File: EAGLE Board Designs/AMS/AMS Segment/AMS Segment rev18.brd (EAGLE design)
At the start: 275.2 x 86 mm, 345 parts, among them J1 CONNECTOR-2_MICROFIT_SMD_RIGH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, J10 CONNECTOR-2_MICROFIT_SMD_RIGH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, J100 CONNECTOR-1_5222, J101 CONNECTOR-1_5222, J102 CONNECTOR-1_5222, J103 CONNECTOR-1_5222, J104 CONNECTOR-1_5222, J105 CONNECTOR-1_5222, J106 CONNECTOR-1_5222, J107 CONNECTOR-1_5222, J108 CONNECTOR-1_5222, J109 CONNECTOR-1_5222, J110 CONNECTOR-1_5222, J111 CONNECTOR-1_5222, J112 CONNECTOR-1_5222, J113 CONNECTOR-1_5222, J114 CONNECTOR-1_5222, J115 CONNECTOR-1_5222, J116 CONNECTOR-1_5222, J117 CONNECTOR-1_5222, J118 CONNECTOR-1_5222, J119 CONNECTOR-1_5222, J120 CONNECTOR-1_5222, J121 CONNECTOR-1_5222, J2 CONNECTOR-2_MICROFIT_SMD_RIGH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, J3 CONNECTOR-2_MICROFIT_SMD_RIGH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, J4 CONNECTOR-2_MICROFIT_SMD_RIGH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, J5 CONNECTOR-2_MICROFIT_SMD_RIGH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, J6 CONNECTOR-2_MICROFIT_SMD_RIGH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, J7 CONNECTOR-2_MICROFIT_SMD_RIGH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, J8 CONNECTOR-2_MICROFIT_SMD_RIGH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, J9 CONNECTOR-2_MICROFIT_SMD_RIGH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, T1 TRANSFORMER_HM2112ZNLT, U1 SHT31-ARP-B, U2 LTC6811-2, U3 LT3990-5, U4 LT3990-5, U5 LTC6811-2, U6 SHT31-ARP-B

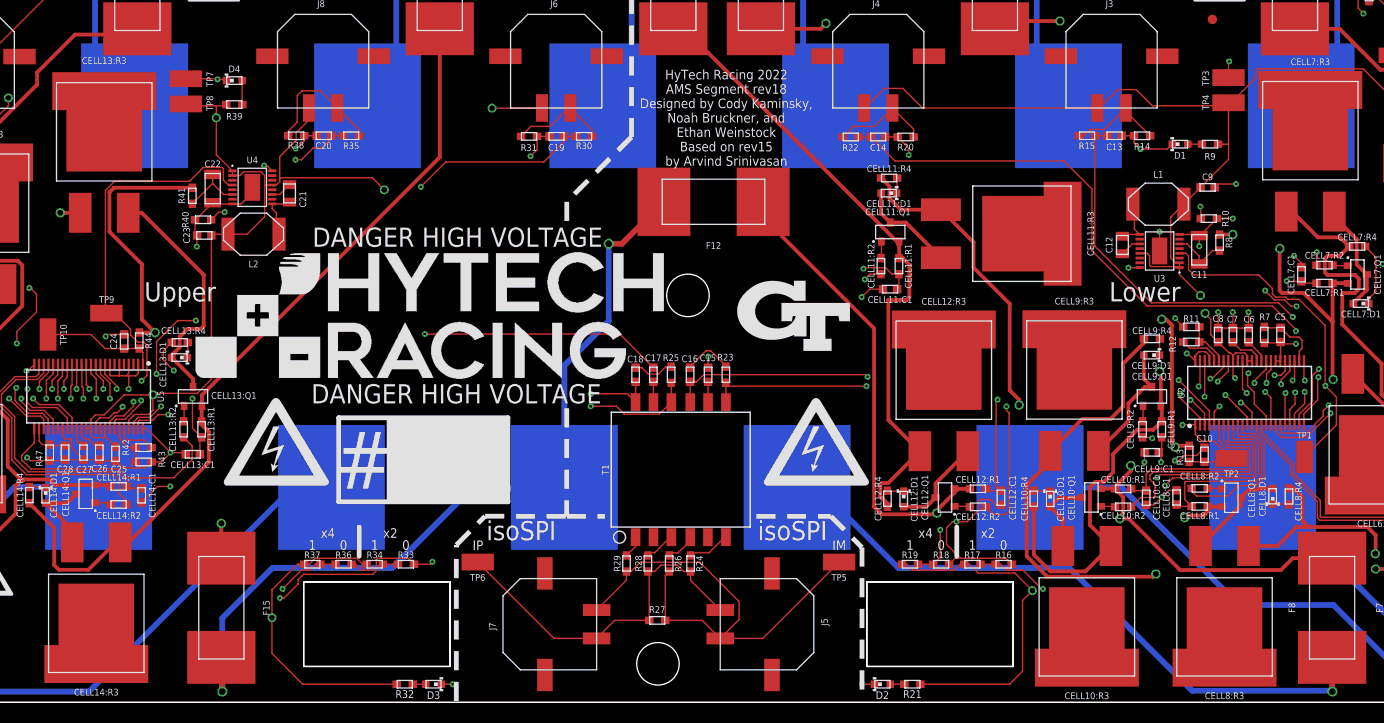
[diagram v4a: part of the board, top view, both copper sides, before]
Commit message: Updated testpoints
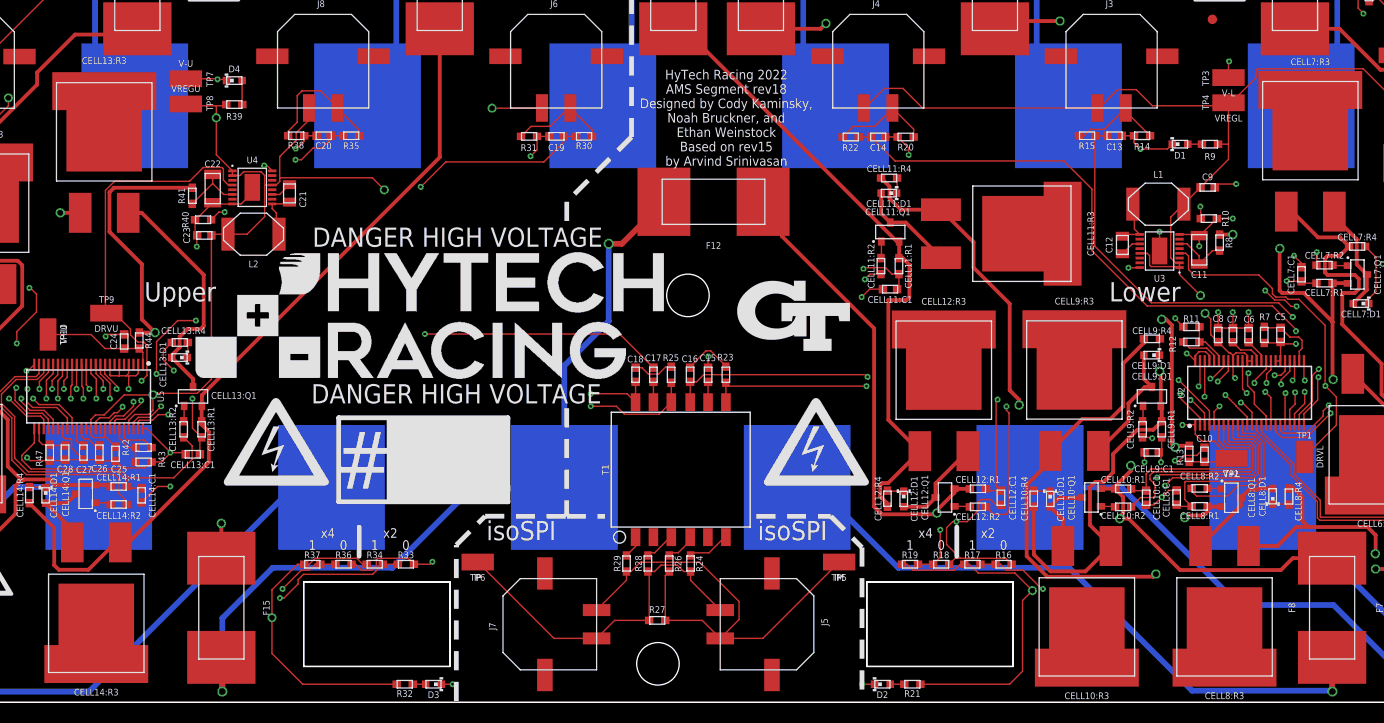
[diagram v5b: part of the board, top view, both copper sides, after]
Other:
- board text removed: "IM"
- board text removed: "IP"
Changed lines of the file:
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@@
 by Arvind Srinivasan
 </text>
-<text x="156.083" y="-69.8754" size="1.016" layer="21" font="vector" align="bottom-center">IM</text>
-<text x="117.856" y="-69.8754" size="1.016" layer="21" font="vector" align="bottom-center">IP</text>
 <rectangle x1="0" y1="-38.1" x2="6.35" y2="-36.83" layer="22" rot="R180"/>
 <rectangle x1="2.54" y1="-40.64" x2="3.81" y2="-34.29" layer="21"/>
@@
 <attribute name="MPN" value="5015" x="78.5368" y="-44.8056" size="0.7112" layer="27" font="vector" rot="R180" display="off"/>
 <attribute name="NAME" x="78.5622" y="-43.7134" size="0.7112" layer="25" font="vector" align="bottom-center"/>
+<attribute name="SIGNAL" value="DRVU" x="78.5368" y="-44.8056" size="1.778" layer="27" rot="R180" display="off"/>
+<attribute name="SIGNAL" value="DRVU" x="78.5368" y="-46.0756" size="0.7112" layer="21" font="vector" rot="R180" align="bottom-center"/>
 </element>
 <element name="TP8" library="HyTechDevices" package="5015" value="TEST_POINT" x="86.9442" y="-22.6695" smashed="yes">
@@
 <attribute name="MPN" value="5015" x="86.9442" y="-22.6695" size="0.7112" layer="27" font="vector" display="off"/>
 <attribute name="NAME" x="89.1286" y="-22.5933" size="0.7112" layer="25" font="vector" rot="R270" align="bottom-center"/>
+<attribute name="SIGNAL" value="VREGU" x="86.9442" y="-22.6695" size="1.778" layer="27" display="off"/>
+<attribute name="SIGNAL" value="VREGU" x="86.9442" y="-21.3995" size="0.7112" layer="21" font="vector" align="bottom-center"/>
 </element>
 <element name="TP1" library="HyTechDevices" package="5015" value="TEST_POINT" x="205.3336" y="-60.0202" smashed="yes" rot="R270">
@@
 <attribute name="MPN" value="5015" x="205.3336" y="-60.0202" size="0.7112" layer="27" font="vector" rot="R270" display="off"/>
 <attribute name="NAME" x="205.3082" y="-58.0644" size="0.7112" layer="25" font="vector" align="bottom-center"/>
+<attribute name="SIGNAL" value="DRVL" x="205.3336" y="-60.0202" size="1.778" layer="27" rot="R270" display="off"/>
+<attribute name="SIGNAL" value="DRVL" x="206.6036" y="-60.0202" size="0.7112" layer="21" font="vector" rot="R270" align="bottom-center"/>
 </element>
 <element name="TP4" library="HyTechDevices" package="5015" value="TEST_POINT" x="197.2818" y="-22.5425" smashed="yes" rot="R180">
@@
 <attribute name="MPN" value="5015" x="197.2818" y="-22.5425" size="0.7112" layer="27" font="vector" rot="R180" display="off"/>
 <attribute name="NAME" x="195.2244" y="-22.4917" size="0.7112" layer="25" font="vector" rot="R90" align="bottom-center"/>
+<attribute name="SIGNAL" value="VREGL" x="197.2818" y="-22.5425" size="1.778" layer="27" rot="R180" display="off"/>
+<attribute name="SIGNAL" value="VREGL" x="197.2818" y="-23.8125" size="0.7112" layer="21" font="vector" rot="R180" align="bottom-center"/>
 </element>
 <element name="TP2" library="HyTechDevices" package="5015" value="TEST_POINT" x="197.5866" y="-60.1726" smashed="yes" rot="R180">
@@
 <attribute name="MPN" value="5015" x="197.5866" y="-60.1726" size="0.7112" layer="27" font="vector" rot="R180" display="off"/>
 <attribute name="NAME" x="197.5866" y="-61.4426" size="0.7112" layer="25" font="vector" rot="R180" align="bottom-center"/>
+<attribute name="SIGNAL" value="V+L" x="197.5866" y="-60.1726" size="1.778" layer="27" rot="R180" display="off"/>
+<attribute name="SIGNAL" value="V+L" x="197.5866" y="-61.4426" size="0.7112" layer="21" font="vector" rot="R180" align="bottom-center"/>
 </element>
 <element name="TP3" library="HyTechDevices" package="5015" value="TEST_POINT" x="197.2818" y="-19.8755" smashed="yes" rot="R180">
@@
 <attribute name="MPN" value="5015" x="197.2818" y="-19.8755" size="0.7112" layer="27" font="vector" rot="R180" display="off"/>
 <attribute name="NAME" x="195.2244" y="-19.9517" size="0.7112" layer="25" font="vector" rot="R90" align="bottom-center"/>
+<attribute name="SIGNAL" value="V-L" x="197.2818" y="-19.8755" size="1.778" layer="27" rot="R180" display="off"/>
+<attribute name="SIGNAL" value="V-L" x="197.2818" y="-21.1455" size="0.7112" layer="21" font="vector" rot="R180" align="bottom-center"/>
 </element>
 <element name="TP10" library="HyTechDevices" package="5015" value="TEST_POINT" x="72.3646" y="-47.0662" smashed="yes" rot="R270">
@@
 <attribute name="MPN" value="5015" x="72.3646" y="-47.0662" size="0.7112" layer="27" font="vector" rot="R270" display="off"/>
 <attribute name="NAME" x="73.6346" y="-47.0662" size="0.7112" layer="25" font="vector" rot="R270" align="bottom-center"/>
+<attribute name="SIGNAL" value="V+U" x="72.3646" y="-47.0662" size="1.778" layer="27" rot="R270" display="off"/>
+<attribute name="SIGNAL" value="V+U" x="73.6346" y="-47.0662" size="0.7112" layer="21" font="vector" rot="R270" align="bottom-center"/>
 </element>
 <element name="TP7" library="HyTechDevices" package="5015" value="TEST_POINT" x="86.9442" y="-20.0025" smashed="yes">
@@
 <attribute name="MPN" value="5015" x="86.9442" y="-20.0025" size="0.7112" layer="27" font="vector" display="off"/>
 <attribute name="NAME" x="89.1286" y="-20.0533" size="0.7112" layer="25" font="vector" rot="R270" align="bottom-center"/>
+<attribute name="SIGNAL" value="V-U" x="86.9442" y="-20.0025" size="1.778" layer="27" display="off"/>
+<attribute name="SIGNAL" value="V-U" x="86.9442" y="-18.7325" size="0.7112" layer="21" font="vector" align="bottom-center"/>
 </element>
 <element name="TP6" library="HyTechDevices" package="5015" value="TEST_POINT" x="117.8306" y="-71.1454" smashed="yes" rot="R180">
@@
 <attribute name="MPN" value="5015" x="117.8306" y="-71.1454" size="0.7112" layer="27" font="vector" rot="R180" display="off"/>
 <attribute name="NAME" x="117.8306" y="-72.4154" size="0.7112" layer="25" font="vector" rot="R180" align="bottom-center"/>
+<attribute name="SIGNAL" value="IP" x="117.8306" y="-71.1454" size="1.778" layer="27" rot="R180" display="off"/>
+<attribute name="SIGNAL" value="IP" x="117.8306" y="-72.4154" size="0.7112" layer="21" font="vector" rot="R180" align="bottom-center"/>
 </element>
 <element name="TP5" library="HyTechDevices" package="5015" value="TEST_POINT" x="156.083" y="-71.1454" smashed="yes" rot="R180">
@@
 <attribute name="MPN" value="5015" x="156.083" y="-71.1454" size="0.7112" layer="27" font="vector" rot="R180" display="off"/>
 <attribute name="NAME" x="156.083" y="-72.4154" size="0.7112" layer="25" font="vector" rot="R180" align="bottom-center"/>
+<attribute name="SIGNAL" value="IM" x="156.083" y="-71.1454" size="1.778" layer="27" rot="R180" display="off"/>
+<attribute name="SIGNAL" value="IM" x="156.083" y="-72.4154" size="0.7112" layer="21" font="vector" rot="R180" align="bottom-center"/>
 </element>
 <element name="U6" library="HyTechDevices" package="DFN-8" value="SHT31-ARP-B" x="49.6062" y="-46.3804" smashed="yes">
@@
 <attribute name="MOPN" value="603-RC0603FR-071KL" x="108.839" y="-87.884" size="1.778" layer="27" rot="R180" display="off"/>
 <attribute name="MPN" value="RC0603FR-071KL" x="108.839" y="-87.884" size="1.778" layer="27" rot="R180" display="off"/>
-<attribute name="NAME" x="110.109" y="-84.709" size="0.8128" layer="25" font="vector" rot="R180" align="bottom-center"/>
+<attribute name="NAME" x="110.109" y="-84.709" size="0.7112" layer="25" font="vector" rot="R180" align="bottom-center"/>
 <attribute name="POWER" value="0.1W" x="108.839" y="-87.884" size="1.778" layer="27" rot="R180" display="off"/>
 <attribute name="RESISTANCE" value="1k" x="108.839" y="-87.884" size="1.778" layer="27" rot="R180" display="off"/>
@@
 <attribute name="MOPN" value="604-APT1608VBC/D" x="111.887" y="-80.264" size="1.778" layer="27" rot="R180" display="off"/>
 <attribute name="MPN" value="APT1608VBC/D" x="111.887" y="-80.264" size="1.778" layer="27" rot="R180" display="off"/>
-<attribute name="NAME" x="113.157" y="-84.824" size="0.8128" layer="25" font="vector" rot="R180" align="bottom-center"/>
+<attribute name="NAME" x="113.157" y="-84.824" size="0.7112" layer="25" font="vector" rot="R180" align="bottom-center"/>
 </element>
 <element name="R21" library="HyTechDevices" package="0603-RES" value="RESISTOR_0603_1K" x="163.83" y="-84.074" smashed="yes">
@@
 <attribute name="MOPN" value="603-RC0603FR-071KL" x="165.1" y="-80.264" size="1.778" layer="27" display="off"/>
 <attribute name="MPN" value="RC0603FR-071KL" x="165.1" y="-80.264" size="1.778" layer="27" display="off"/>
-<attribute name="NAME" x="163.83" y="-84.709" size="0.8128" layer="25" font="vector" align="top-center"/>
+<attribute name="NAME" x="163.83" y="-84.709" size="0.7112" layer="25" font="vector" align="top-center"/>
 <attribute name="POWER" value="0.1W" x="165.1" y="-80.264" size="1.778" layer="27" display="off"/>
 <attribute name="RESISTANCE" value="1k" x="165.1" y="-80.264" size="1.778" layer="27" display="off"/>
@@
 <attribute name="MOPN" value="604-APT1608VBC/D" x="161.925" y="-87.884" size="1.778" layer="27" display="off"/>
 <attribute name="MPN" value="APT1608VBC/D" x="161.925" y="-87.884" size="1.778" layer="27" display="off"/>
-<attribute name="NAME" x="160.655" y="-84.824" size="0.8128" layer="25" font="vector" align="top-center"/>
+<attribute name="NAME" x="160.655" y="-84.824" size="0.7112" layer="25" font="vector" align="top-center"/>
 </element>
 <element name="U$19" library="HyTechAesthetics" package="LOGO_HYTECH_LARGE" value="" x="87.884" y="-51.689" smashed="yes"/>
